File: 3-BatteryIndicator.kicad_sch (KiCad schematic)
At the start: 10 parts, among them J301 2.54mm header, U301 MMDT2222A-7-F

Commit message: improving the schematic - v3.0. Very crude draft of board layout with battery holder underneath the PCB
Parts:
- removed J301: 2.54mm header, library:77311-818-02, symbol Connector:Conn_01x02_Pin
- removed R304: 3k9, library:ERA-3AEB392V, symbol Device:R_Small
- removed RV302: trim B10k, library:ST-4ETB103, symbol Device:R_Potentiometer_Trim
- added R?: 10k, library:RT0603BRD0710KL, symbol Device:R_Small
- added S301: OS102011MA1QN1, library:OS102011MA1QN1, symbol OS102011MA1QN1:OS102011MA1QN1
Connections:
- net BI_C1: now also R?.2
- net BI_SW: now also S301.3
- net LED_K: now also R?.1
- net Vbi: now also S301.2
- no-connect marks 0 -> 1
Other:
- note added: "I = (20-1.5)V / 10000 = 1.85mA max"
- note added: "POWER-ON LED MODE SWITCH"
- note added: "Power-on LED mode switch goes here"
- note added: "alt (same footprint): OS102011MA1QN1C OS102011MA1QS1 OS102011MA1QS1C alt (different footprint): 1825232-1"
- note added: "left = closed = NC = "Battery indicator mode" right = open = NO = "LED always on""
- note removed: "BI mode switch"
- note removed: "I = (20-1.5)V / 3k9 = <5mA, which is max wiper current"
- note removed: "Power-on LED intensity adjustment"
- note removed: "alt: DIP sw"
- note removed: "open = "LED always on" closed = "BI""
- moved on the sheet: C?, D301, R301, R302, R303, RV301

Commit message: saving in Kicad8 for the first time - some underlying formats changed
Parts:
- gave numbers to parts that had none: 2

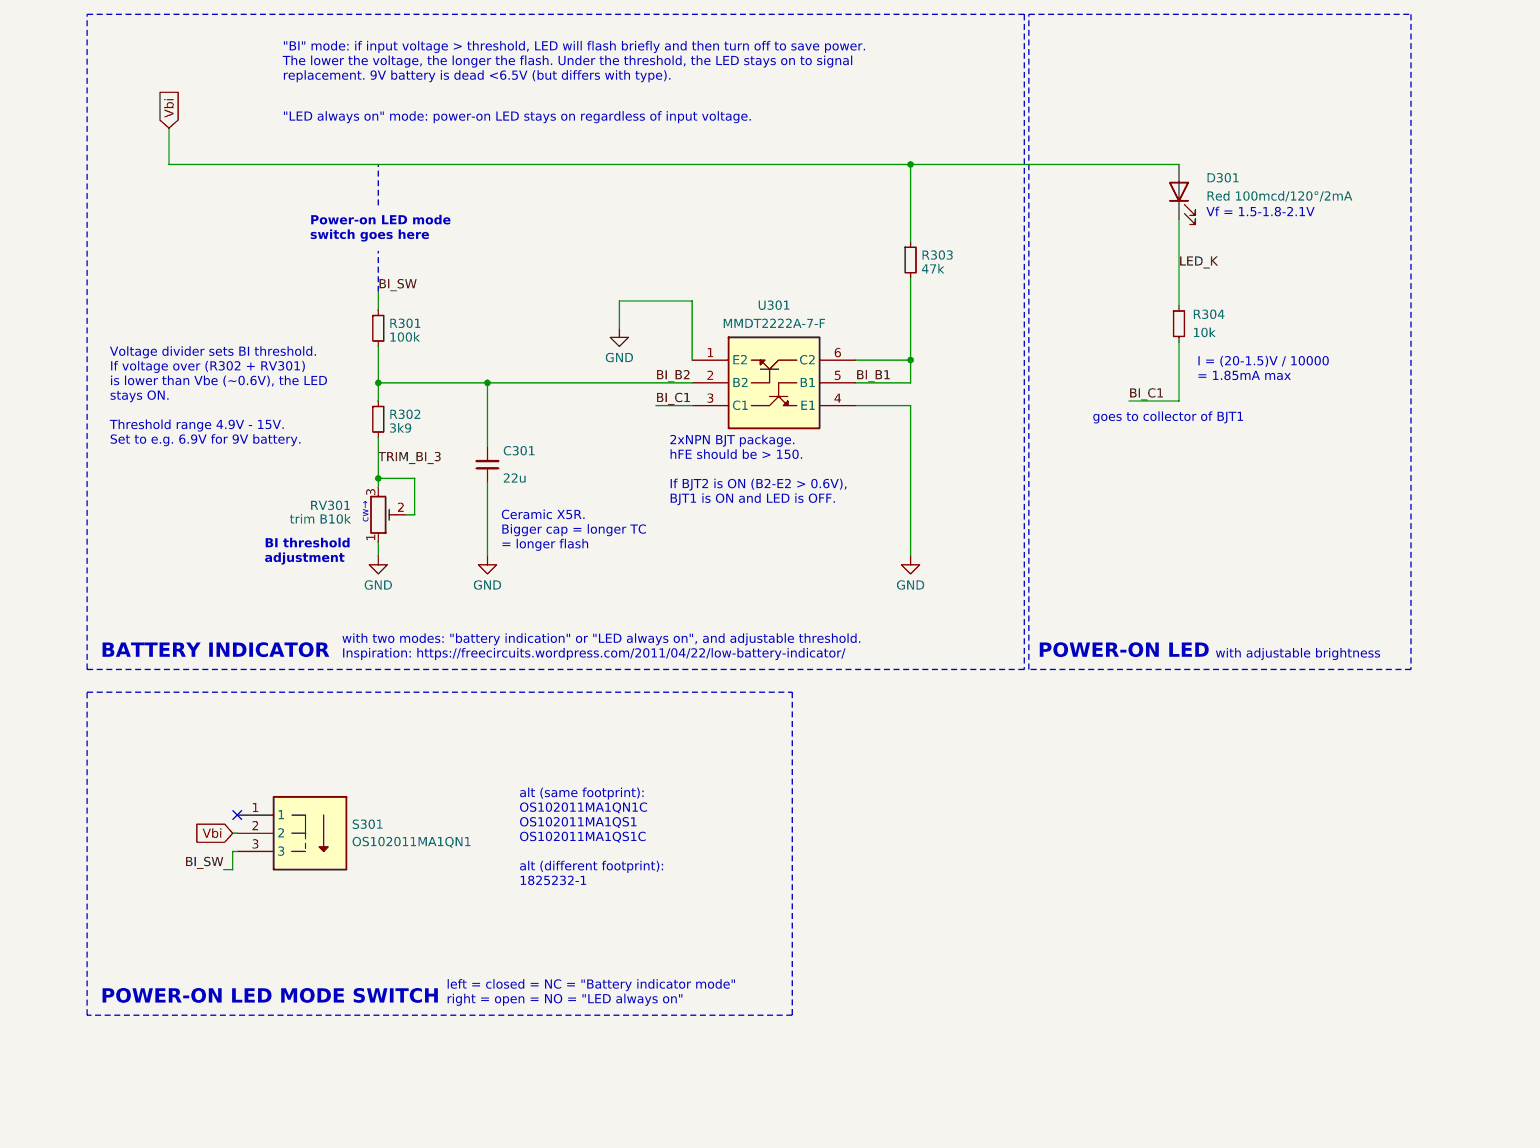
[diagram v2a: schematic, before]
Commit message: schematics: heavy BOM optimization, many small changes, filling missing fields, improving symbols and everything
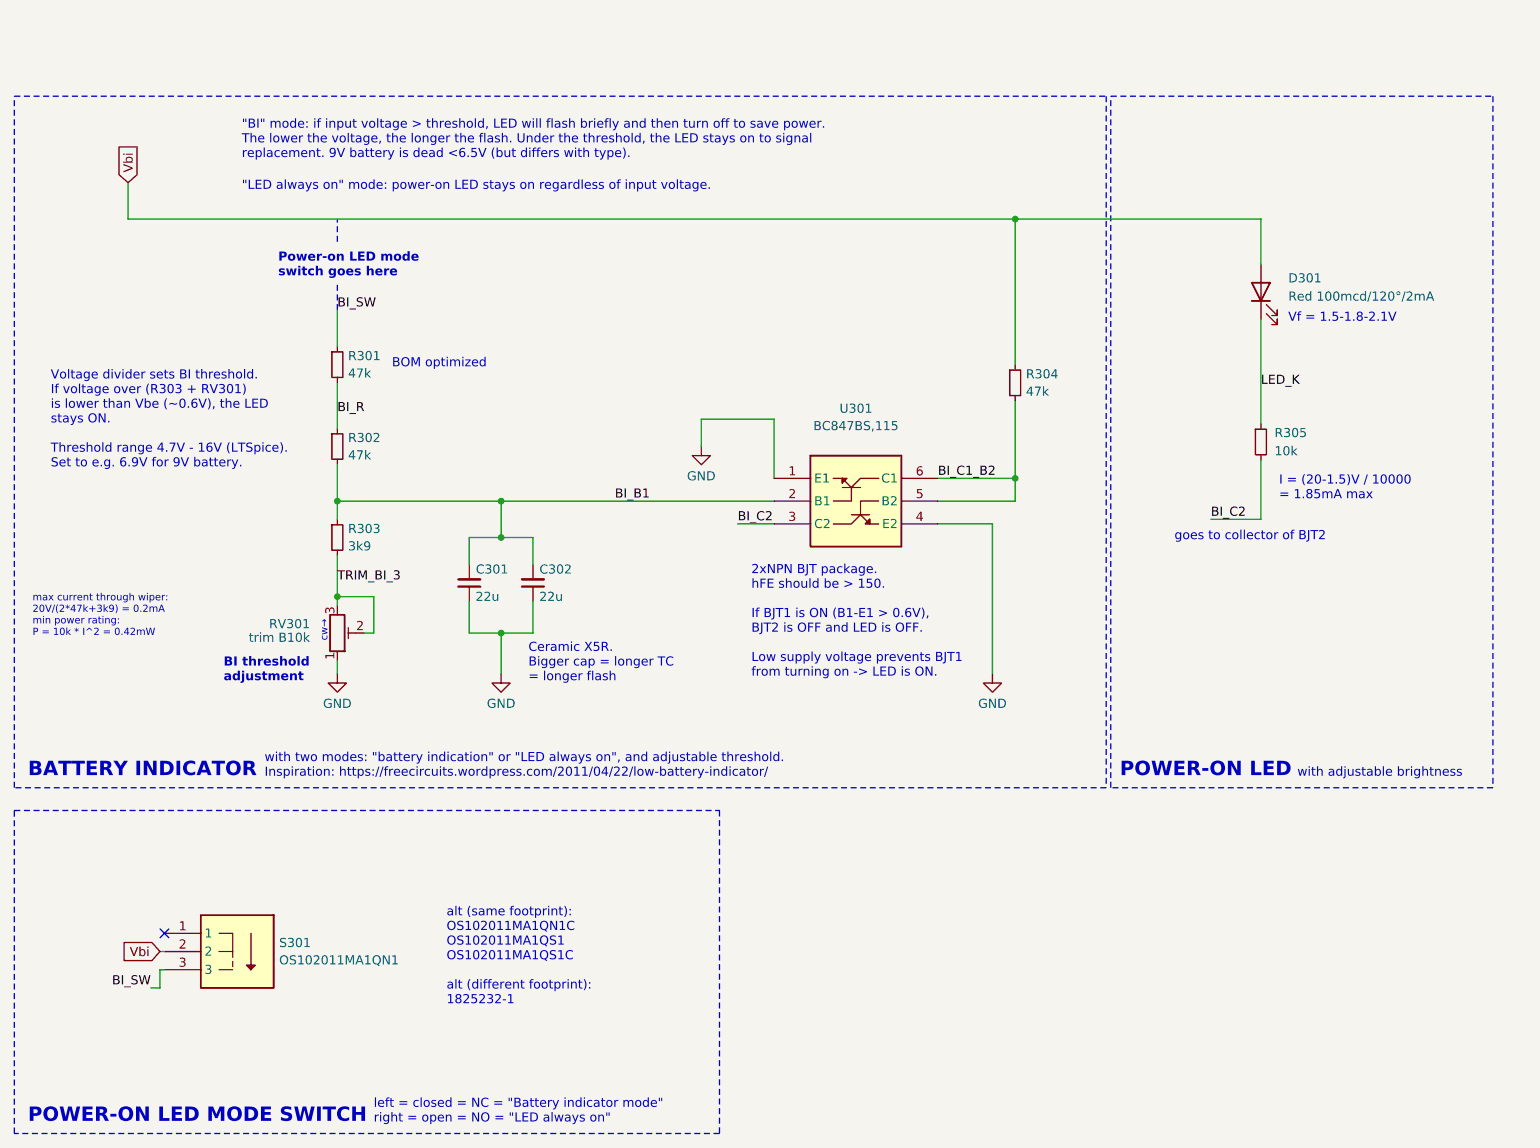
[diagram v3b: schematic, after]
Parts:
- removed U301: MMDT2222A-7-F, library:MMDT2222A-7-F, symbol MMDT2222A-7-F:MMDT2222A-7-F
- added C302: 22u, library:cap_CL31A226KAHNNNE, symbol Device:C_Small
- added R302: 47k, library:RT0603BRD0747KL, symbol Device:R_Small
- added U301: BC847BS,115, library:bjt_BC847BS_115, symbol bjt_BC847BS_115:BC847BS,115
- C301: footprint library:GRM21BR61E226ME44L -> library:cap_CL31A226KAHNNNE; LCSC Part # C86816 -> C12891; Mfr Murata -> Samsung; Mfr Part # GRM21BR61E226ME44L -> CL31A226KAHNNNE; Mouser Part # 81-GRM21BR61E226ME4L -> 187-CL31A226KAHNNNE; Source (none) -> LCSC
- D301: Source (none) -> LCSC
- R301: value 100k -> 47k; footprint library:RT0603BRD07100KL -> library:RT0603BRD0747KL; LCSC Part # C122538 -> C326725; Mfr Part # RT0603BRD07100KL -> RT0603BRD0747KL; Mouser Part # 603-RT0603BRD07100KL -> 603-RT0603BRD0747KL; Purpose BI - threshold voltage divider -> BI - threshold voltage divider (BOM optimized); Source (none) -> LCSC
- R303: renamed from R302; Source (none) -> LCSC
- R304: renamed from R303; Source (none) -> LCSC
- R305: renamed from R304; Source (none) -> LCSC
- RV301: footprint library:ST-4ETB103 -> library:trimpot_TC33X-2-103E; LCSC Part # C2922095 -> C719176; Mfr Nidec -> Bourns; Mfr Part # ST-4ETB103 -> TC33X-2-103E; Mouser Part # 229-ST-4ETB103 -> 652-TC33X-2-103E; Source (none) -> LCSC
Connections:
- net BI_B1: now also C301.2, R303.1, C302.2, R302.2, U301.2 (B1); no longer R304.2
- net GND: now also C302.1, U301.1 (E1), U301.4 (E2)
- removed net BI_B2: C301.2, R301.2, R303.1
- net BI_C1 renamed BI_C2
- net BI_C2: now also U301.3 (C2)
- new net BI_C1_B2: R304.2, U301.5 (B2), U301.6 (C1)
- new net BI_R: R301.2, R302.1
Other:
- note added: "2xNPN BJT package. hFE should be > 150. If BJT1 is ON (B1-E1 > 0.6V), BJT2 is OFF and LED is OFF. Low supply voltage prevents BJT1 from turning on -> LED is ON."
- note added: "BOM optimized"
- note added: "Voltage divider sets BI threshold. If voltage over (R303 + RV301) is lower than Vbe (~0.6V), the LED stays ON. Threshold range 4.7V - 16V (LTSpice). Set to e.g. 6.9V for 9V battery."
- note added: "goes to collector of BJT2"
- note added: "max current through wiper: 20V/(2*47k+3k9) = 0.2mA min power rating: P = 10k * I^2 = 0.42mW"
- note removed: "2xNPN BJT package. hFE should be > 150. If BJT2 is ON (B2-E2 > 0.6V), BJT1 is ON and LED is OFF."
- note removed: "Voltage divider sets BI threshold. If voltage over (R302 + RV301) is lower than Vbe (~0.6V), the LED stays ON. Threshold range 4.9V - 15V. Set to e.g. 6.9V for 9V battery."
- note removed: "goes to collector of BJT1"
- moved on the sheet: C301, D301, R303, R304, R305, RV301, S301

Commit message: aligning schematics to grid, swapping switches as they are on the bottom side now; rough placement of BI section on board
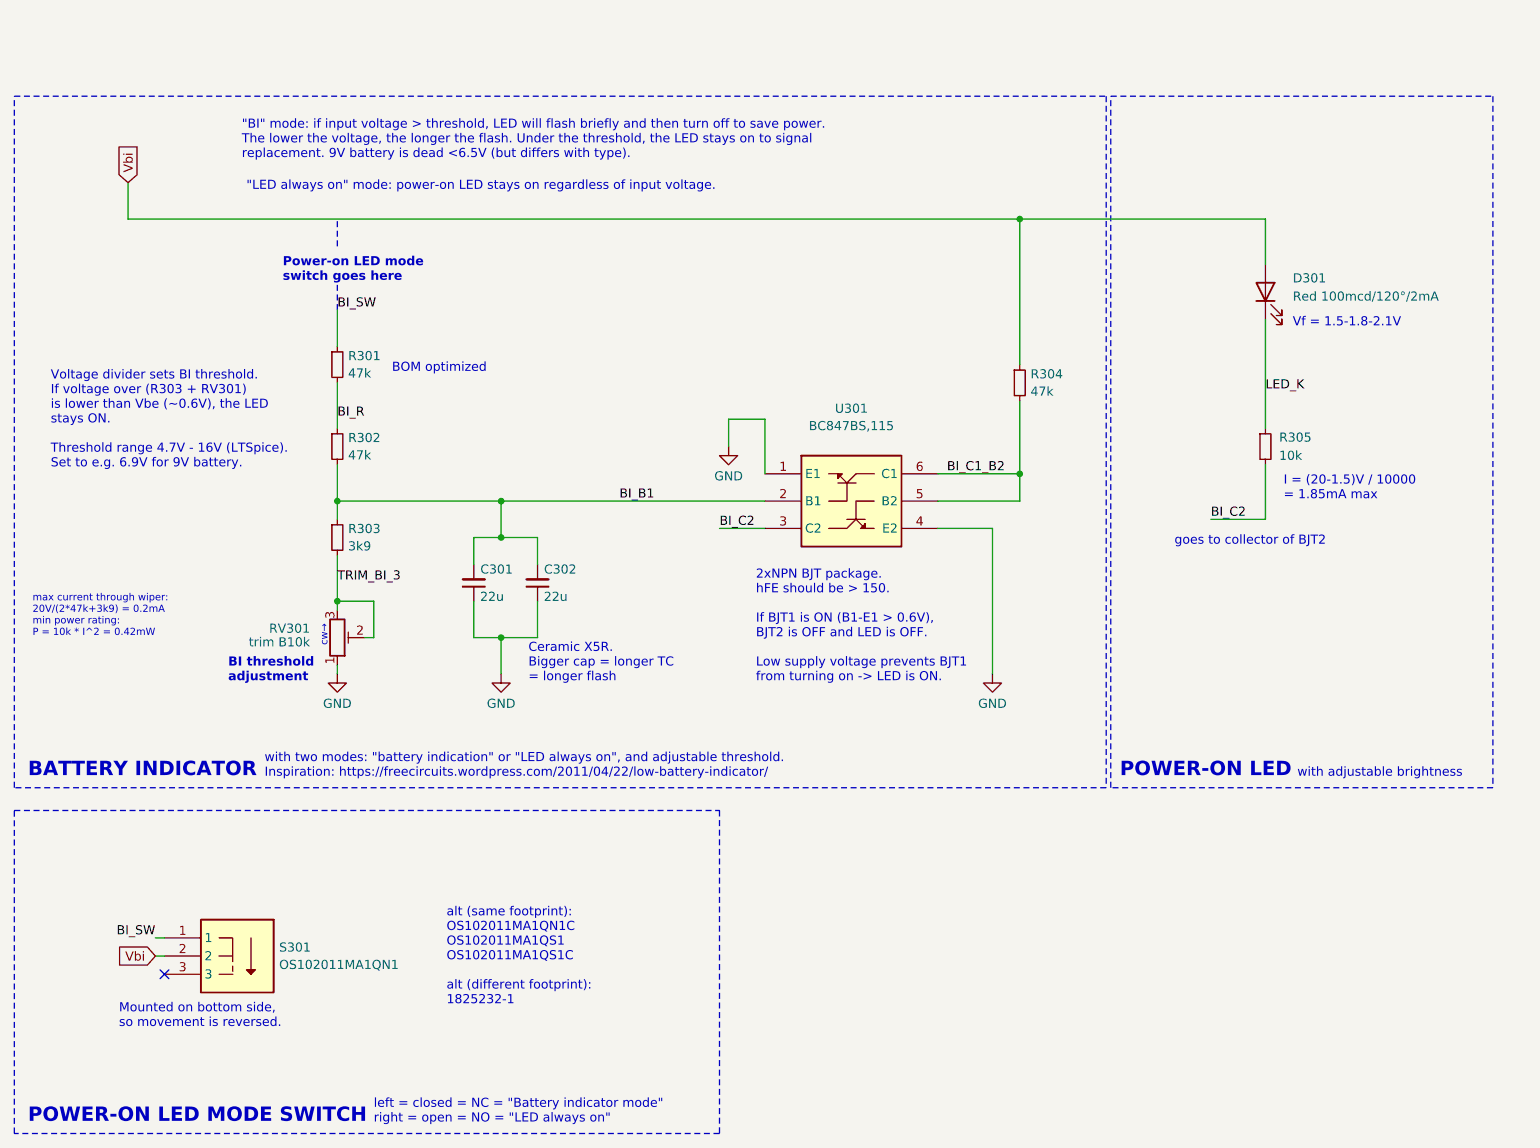
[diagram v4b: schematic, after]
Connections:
- net BI_SW: now also S301.1; no longer S301.3
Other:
- note added: "Mounted on bottom side, so movement is reversed."
- moved on the sheet: C301, C302, D301, R304, R305, RV301, S301, U301

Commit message: schematics: replacing the switches, rewiring, improving center switch positions, removing 6n8 cap
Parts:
- S301: Source (none) -> Mouser
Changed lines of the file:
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@@
 			)
 		)
-		(property "Source" ""
+		(property "Source" "Mouser"
 			(at 66.04 151.13 0)
 			(effects
